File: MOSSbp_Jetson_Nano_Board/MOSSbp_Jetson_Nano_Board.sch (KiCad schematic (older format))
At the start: 49 parts, among them J1 24V, J10 Temp2, J2 Circulation Fan, J3 CO2, J4 Water Pump PWM, J5 Vent Fan, J6 Water Pump, J7 I2C, J8 Jetson_Nano_Dev, J9 Temp1, Q1 DMN3404L, Q2 DMN3404L, Q3 BSS138, Q4 DMN3404L, U1 MIC4416, U2 MIC4416, U3 LMR14020, U4 PTN78020WAH, U5 MIC4416

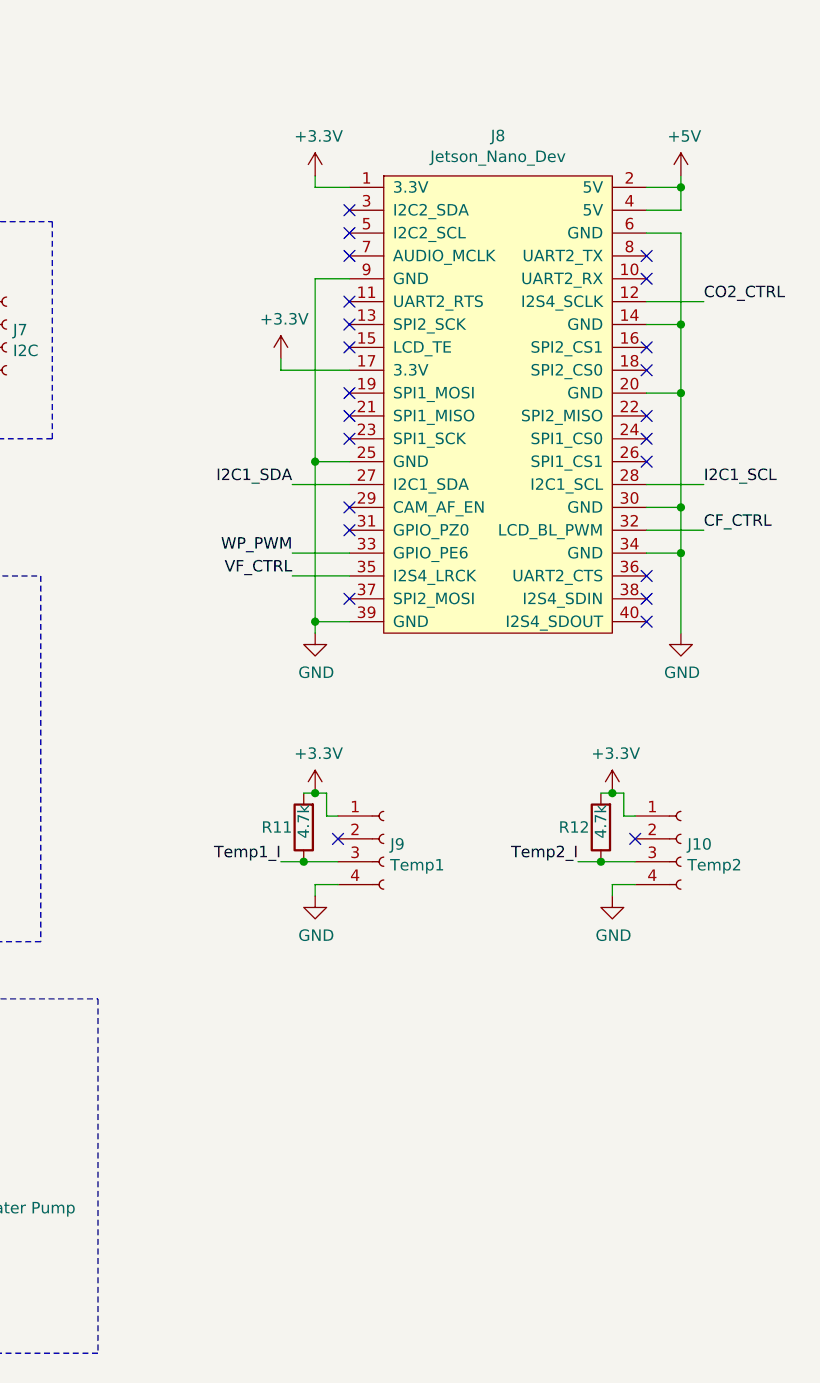
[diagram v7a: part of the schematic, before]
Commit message: Finished adding temp sensors
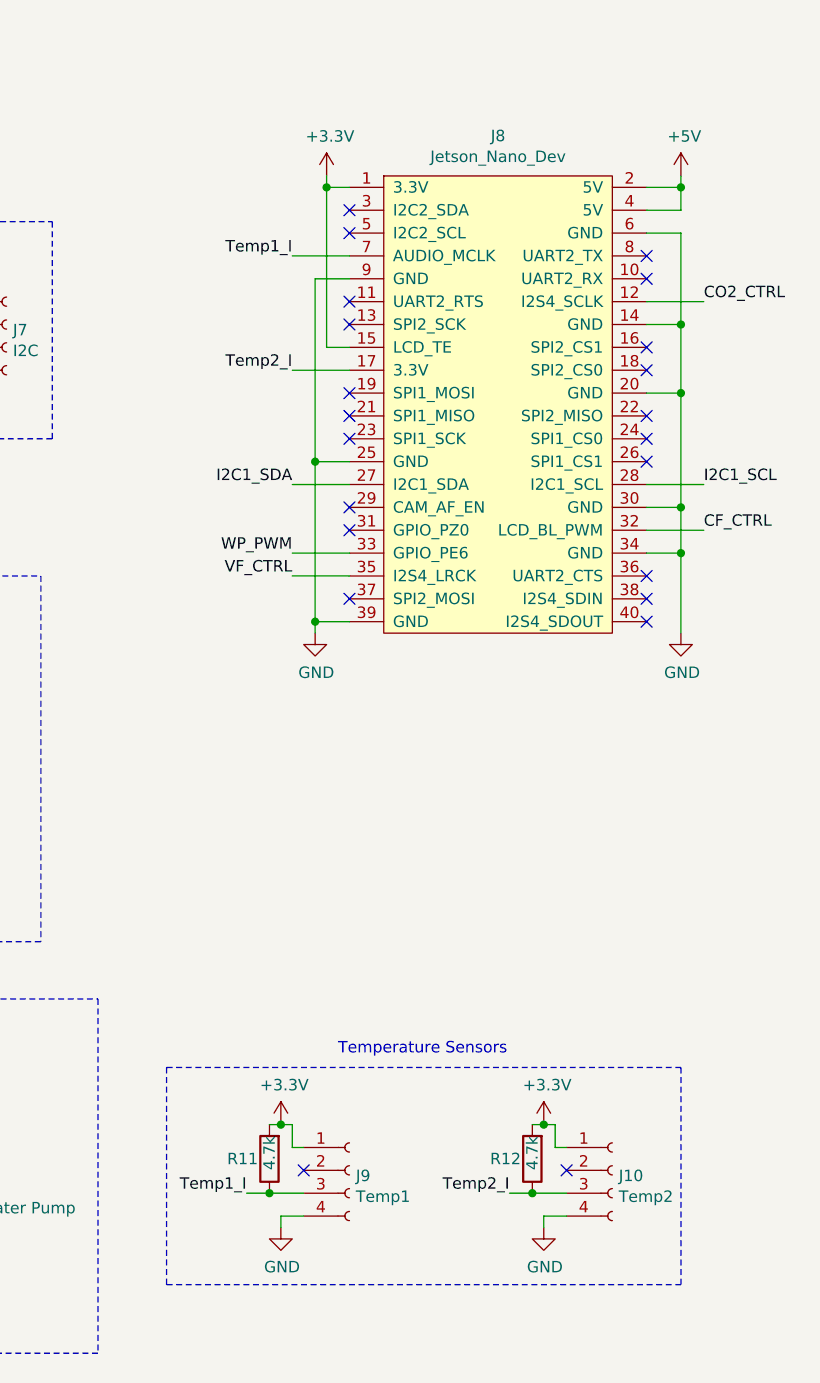
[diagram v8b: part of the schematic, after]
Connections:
- net +3V3: now also J8.15 (LCD_TE); no longer J8.17 (3.3V)
- net Temp1_I: now also J8.7 (AUDIO_MCLK)
- net Temp2_I: now also J8.17 (3.3V)
- no-connect marks 26 -> 24
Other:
- note added: "Temperature Sensors"
- moved on the sheet: J10, J9, R11, R12
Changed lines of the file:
@@
 NoConn ~ 8600 1400
 NoConn ~ 8600 1500
-NoConn ~ 8600 1600
 NoConn ~ 8600 1800
-NoConn ~ 8600 1900
-NoConn ~ 8600 2000
 NoConn ~ 8600 2200
 NoConn ~ 8600 2300
@@
 L power:+3.3V #PWR039
 U 1 1 5E099D1C
-P 8450 1250
-F 0 "#PWR039" H 8450 1100 50  0001 C CNN
-F 1 "+3.3V" H 8465 1423 50  0000 C CNN
-F 2 "" H 8450 1250 50  0001 C CNN
-F 3 "" H 8450 1250 50  0001 C CNN
-	1    8450 1250
+P 8500 1250
+F 0 "#PWR039" H 8500 1100 50  0001 C CNN
+F 1 "+3.3V" H 8515 1423 50  0000 C CNN
+F 2 "" H 8500 1250 50  0001 C CNN
+F 3 "" H 8500 1250 50  0001 C CNN
+	1    8500 1250
 	1    0    0    -1
 $EndComp
@@
 $EndComp
 Wire Wire Line
-	8600 1300 8450 1300
-Wire Wire Line
-	8450 1300 8450 1250
+	8600 1300 8500 1300
 Wire Wire Line
 	8600 3200 8450 3200
@@
 Wire Wire Line
 	8450 1700 8450 2500
-$Comp
-L power:+3.3V #PWR038
-U 1 1 5E09C0FA
-P 8300 2050
-F 0 "#PWR038" H 8300 1900 50  0001 C CNN
-F 1 "+3.3V" H 8315 2223 50  0000 C CNN
-F 2 "" H 8300 2050 50  0001 C CNN
-F 3 "" H 8300 2050 50  0001 C CNN
-	1    8300 2050
-	1    0    0    -1
-$EndComp
-Wire Wire Line
-	8600 2100 8300 2100
-Wire Wire Line
-	8300 2100 8300 2050
 $Comp
 L power:+5V #PWR041
@@
 L power:+3.3V #PWR045
 U 1 1 5E3028DE
-P 9750 3950
-F 0 "#PWR045" H 9750 3800 50  0001 C CNN
-F 1 "+3.3V" H 9765 4123 50  0000 C CNN
-F 2 "" H 9750 3950 50  0001 C CNN
-F 3 "" H 9750 3950 50  0001 C CNN
-	1    9750 3950
+P 9450 5400
+F 0 "#PWR045" H 9450 5250 50  0001 C CNN
+F 1 "+3.3V" H 9465 5573 50  0000 C CNN
+F 2 "" H 9450 5400 50  0001 C CNN
+F 3 "" H 9450 5400 50  0001 C CNN
+	1    9450 5400
 	1    0    0    -1
 $EndComp
@@
 L power:GND #PWR046
 U 1 1 5E3028E8
-P 9750 4400
-F 0 "#PWR046" H 9750 4150 50  0001 C CNN
-F 1 "GND" H 9755 4227 50  0000 C CNN
-F 2 "" H 9750 4400 50  0001 C CNN
-F 3 "" H 9750 4400 50  0001 C CNN
-	1    9750 4400
-	1    0    0    -1
-$EndComp
-Wire Wire Line
-	9850 4350 9750 4350
-Wire Wire Line
-	9750 4350 9750 4400
+P 9450 5850
+F 0 "#PWR046" H 9450 5600 50  0001 C CNN
+F 1 "GND" H 9455 5677 50  0000 C CNN
+F 2 "" H 9450 5850 50  0001 C CNN
+F 3 "" H 9450 5850 50  0001 C CNN
+	1    9450 5850
+	1    0    0    -1
+$EndComp
+Wire Wire Line
+	9550 5800 9450 5800
+Wire Wire Line
+	9450 5800 9450 5850
 $Comp
 L Connector:Conn_01x04_Female J10
 U 1 1 5E3028F9
-P 10050 4150
-F 0 "J10" H 10078 4126 50  0000 L CNN
-F 1 "Temp2" H 10078 4035 50  0000 L CNN
-F 2 "Connector_JST:JST_GH_BM04B-GHS-TBT_1x04-1MP_P1.25mm_Vertical" H 10050 4150 50  0001 C CNN
-F 3 "~" H 10050 4150 50  0001 C CNN
-F 4 "455-1580-1-ND" H 10050 4150 50  0001 C CNN "Digi-Key_PN"
-	1    10050 4150
+P 9750 5600
+F 0 "J10" H 9778 5576 50  0000 L CNN
+F 1 "Temp2" H 9778 5485 50  0000 L CNN
+F 2 "Connector_JST:JST_GH_BM04B-GHS-TBT_1x04-1MP_P1.25mm_Vertical" H 9750 5600 50  0001 C CNN
+F 3 "~" H 9750 5600 50  0001 C CNN
+F 4 "455-1580-1-ND" H 9750 5600 50  0001 C CNN "Digi-Key_PN"
+	1    9750 5600
 	1    0    0    -1
 $EndComp
@@
 L Device:R R12
 U 1 1 5E32BEDB
-P 9700 4100
-F 0 "R12" H 9750 4100 50  0000 L CNN
-F 1 "4.7k" V 9700 4000 50  0000 L CNN
-F 2 "Resistor_SMD:R_0603_1608Metric_Pad1.05x0.95mm_HandSolder" V 9630 4100 50  0001 C CNN
-F 3 "~" H 9700 4100 50  0001 C CNN
-F 4 "311-4.7KGRCT-ND" H 9700 4100 50  0001 C CNN "Digi-Key_PN"
-	1    9700 4100
+P 9400 5550
+F 0 "R12" H 9450 5550 50  0000 L CNN
+F 1 "4.7k" V 9400 5450 50  0000 L CNN
+F 2 "Resistor_SMD:R_0603_1608Metric_Pad1.05x0.95mm_HandSolder" V 9330 5550 50  0001 C CNN
+F 3 "~" H 9400 5550 50  0001 C CNN
+F 4 "311-4.7KGRCT-ND" H 9400 5550 50  0001 C CNN "Digi-Key_PN"
+	1    9400 5550
 	-1   0    0    1
 $EndComp
 Wire Wire Line
-	9850 4050 9800 4050
-Wire Wire Line
-	9800 4050 9800 3950
-Wire Wire Line
-	9800 3950 9750 3950
-Wire Wire Line
-	9850 4250 9700 4250
-Connection ~ 9700 4250
-Wire Wire Line
-	9700 4250 9600 4250
-Connection ~ 9750 3950
-Wire Wire Line
-	9750 3950 9700 3950
-NoConn ~ 9850 4150
-Text Label 9600 4250 2    50   ~ 0
+	9550 5500 9500 5500
+Wire Wire Line
+	9500 5500 9500 5400
+Wire Wire Line
+	9500 5400 9450 5400
+Wire Wire Line
+	9550 5700 9400 5700
+Connection ~ 9400 5700
+Wire Wire Line
+	9400 5700 9300 5700
+Connection ~ 9450 5400
+Wire Wire Line
+	9450 5400 9400 5400
+NoConn ~ 9550 5600
+Text Label 9300 5700 2    50   ~ 0
 Temp2_I
 $Comp
 L power:+3.3V #PWR043
 U 1 1 5E3B00BB
-P 8450 3950
-F 0 "#PWR043" H 8450 3800 50  0001 C CNN
-F 1 "+3.3V" H 8465 4123 50  0000 C CNN
-F 2 "" H 8450 3950 50  0001 C CNN
-F 3 "" H 8450 3950 50  0001 C CNN
-	1    8450 3950
+P 8300 5400
+F 0 "#PWR043" H 8300 5250 50  0001 C CNN
+F 1 "+3.3V" H 8315 5573 50  0000 C CNN
+F 2 "" H 8300 5400 50  0001 C CNN
+F 3 "" H 8300 5400 50  0001 C CNN
+	1    8300 5400
 	1    0    0    -1
 $EndComp
@@
 L power:GND #PWR044
 U 1 1 5E3B00C5
-P 8450 4400
-F 0 "#PWR044" H 8450 4150 50  0001 C CNN
-F 1 "GND" H 8455 4227 50  0000 C CNN
-F 2 "" H 8450 4400 50  0001 C CNN
-F 3 "" H 8450 4400 50  0001 C CNN
-	1    8450 4400
-	1    0    0    -1
-$EndComp
-Wire Wire Line
-	8550 4350 8450 4350
-Wire Wire Line
-	8450 4350 8450 4400
+P 8300 5850
+F 0 "#PWR044" H 8300 5600 50  0001 C CNN
+F 1 "GND" H 8305 5677 50  0000 C CNN
+F 2 "" H 8300 5850 50  0001 C CNN
+F 3 "" H 8300 5850 50  0001 C CNN
+	1    8300 5850
+	1    0    0    -1
+$EndComp
+Wire Wire Line
+	8400 5800 8300 5800
+Wire Wire Line
+	8300 5800 8300 5850
 $Comp
 L Connector:Conn_01x04_Female J9
 U 1 1 5E3B00D2
-P 8750 4150
-F 0 "J9" H 8778 4126 50  0000 L CNN
-F 1 "Temp1" H 8778 4035 50  0000 L CNN
-F 2 "Connector_JST:JST_GH_BM04B-GHS-TBT_1x04-1MP_P1.25mm_Vertical" H 8750 4150 50  0001 C CNN
-F 3 "~" H 8750 4150 50  0001 C CNN
-F 4 "455-1580-1-ND" H 8750 4150 50  0001 C CNN "Digi-Key_PN"
-	1    8750 4150
+P 8600 5600
+F 0 "J9" H 8628 5576 50  0000 L CNN
+F 1 "Temp1" H 8628 5485 50  0000 L CNN
+F 2 "Connector_JST:JST_GH_BM04B-GHS-TBT_1x04-1MP_P1.25mm_Vertical" H 8600 5600 50  0001 C CNN
+F 3 "~" H 8600 5600 50  0001 C CNN
+F 4 "455-1580-1-ND" H 8600 5600 50  0001 C CNN "Digi-Key_PN"
+	1    8600 5600
 	1    0    0    -1
 $EndComp
@@
 L Device:R R11
 U 1 1 5E3B00DD
-P 8400 4100
-F 0 "R11" H 8450 4100 50  0000 L CNN
-F 1 "4.7k" V 8400 4000 50  0000 L CNN
-F 2 "Resistor_SMD:R_0603_1608Metric_Pad1.05x0.95mm_HandSolder" V 8330 4100 50  0001 C CNN
-F 3 "~" H 8400 4100 50  0001 C CNN
-F 4 "311-4.7KGRCT-ND" H 8400 4100 50  0001 C CNN "Digi-Key_PN"
-	1    8400 4100
+P 8250 5550
+F 0 "R11" H 8300 5550 50  0000 L CNN
+F 1 "4.7k" V 8250 5450 50  0000 L CNN
+F 2 "Resistor_SMD:R_0603_1608Metric_Pad1.05x0.95mm_HandSolder" V 8180 5550 50  0001 C CNN
+F 3 "~" H 8250 5550 50  0001 C CNN
+F 4 "311-4.7KGRCT-ND" H 8250 5550 50  0001 C CNN "Digi-Key_PN"
+	1    8250 5550
 	-1   0    0    1
 $EndComp
 Wire Wire Line
-	8550 4050 8500 4050
-Wire Wire Line
-	8500 4050 8500 3950
-Wire Wire Line
-	8500 3950 8450 3950
-Wire Wire Line
-	8550 4250 8400 4250
-Connection ~ 8400 4250
-Wire Wire Line
-	8400 4250 8300 4250
-Connection ~ 8450 3950
-Wire Wire Line
-	8450 3950 8400 3950
-NoConn ~ 8550 4150
-Text Label 8300 4250 2    50   ~ 0
+	8400 5500 8350 5500
+Wire Wire Line
+	8350 5500 8350 5400
+Wire Wire Line
+	8350 5400 8300 5400
+Wire Wire Line
+	8400 5700 8250 5700
+Connection ~ 8250 5700
+Wire Wire Line
+	8250 5700 8150 5700
+Connection ~ 8300 5400
+Wire Wire Line
+	8300 5400 8250 5400
+NoConn ~ 8400 5600
+Text Label 8150 5700 2    50   ~ 0
 Temp1_I
+Wire Notes Line
+	10050 5150 10050 6100
+Wire Notes Line
+	7800 6100 10050 6100
+Wire Notes Line
+	7800 5150 10050 5150
+Wire Notes Line
+	7800 6100 7800 5150
+Text Notes 8550 5100 0    50   ~ 0
+Temperature Sensors
+Text Label 8350 1600 2    50   ~ 0
+Temp1_I
+NoConn ~ 8600 1900
+Wire Wire Line
+	8600 2000 8500 2000
+Wire Wire Line
+	8500 2000 8500 1300
+Wire Wire Line
+	8500 1300 8500 1250
+Connection ~ 8500 1300
+Wire Wire Line
+	8350 2100 8600 2100
+Text Label 8350 2100 2    50   ~ 0
+Temp2_I
+Wire Wire Line
+	8350 1600 8600 1600
 $EndSCHEMATC
